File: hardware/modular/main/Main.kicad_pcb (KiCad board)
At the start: 4 copper layers, 80 x 125 mm, 246 parts, among them J1 TYPE-C-31-M-12, J10 Soldered wires Power_1x02, J2 Soldered wires Power_1x02, J3 Soldered wires Power_1x02, J4 Soldered wires Power_1x02, J6 Soldered wires Signal_2x04, J8 Soldered wires Signal_2x15, Q1 2N7002, Q2 2N7002, Q3 2N7002, SW1 RESET, SW2 BOOT, U1 TPD2EUSB30DRTR, U10 ADS7038IRTER, U11 TUSB320LAIRWBR, U12 TPS259470LRPWR, U13 TPS259470LRPWR, U14 SN74LVC2G04DCKR, U15 SN74LVC1G123DCUR, U16 SN74LVC08APWR, U17 SN74LVC08APWR, U18 SN74LVC08APWR, U19 TLV9001IDBVR, U2 TPS62162DSGR, U20 TPD2E2U06DCKR, U25 SN74LVC125APWR, U28 TPS22919DCKR, U29 SN74LVC125APWR, U3 ESP32-S3-MINI-1-N8, U32 ICM-42688-P, U33 TPS7A2450DBVR, U34 SN74LV1T34DBVR, U35 PMW3360DM-T2QU, U36 TLV75519PDBVR, U37 SN74LVC125APWR, U38 TPS22918DBVR, U39 SN74LVC1G125DBVR, U4 DRV8231ADSGR, U5 DRV8231ADSGR, U6 DRV8231ADSGR, U7 TMAG5253BA2IQDMRR, U8 TMAG5253BA2IQDMRR, U9 TMAG5253BA2IQDMRR

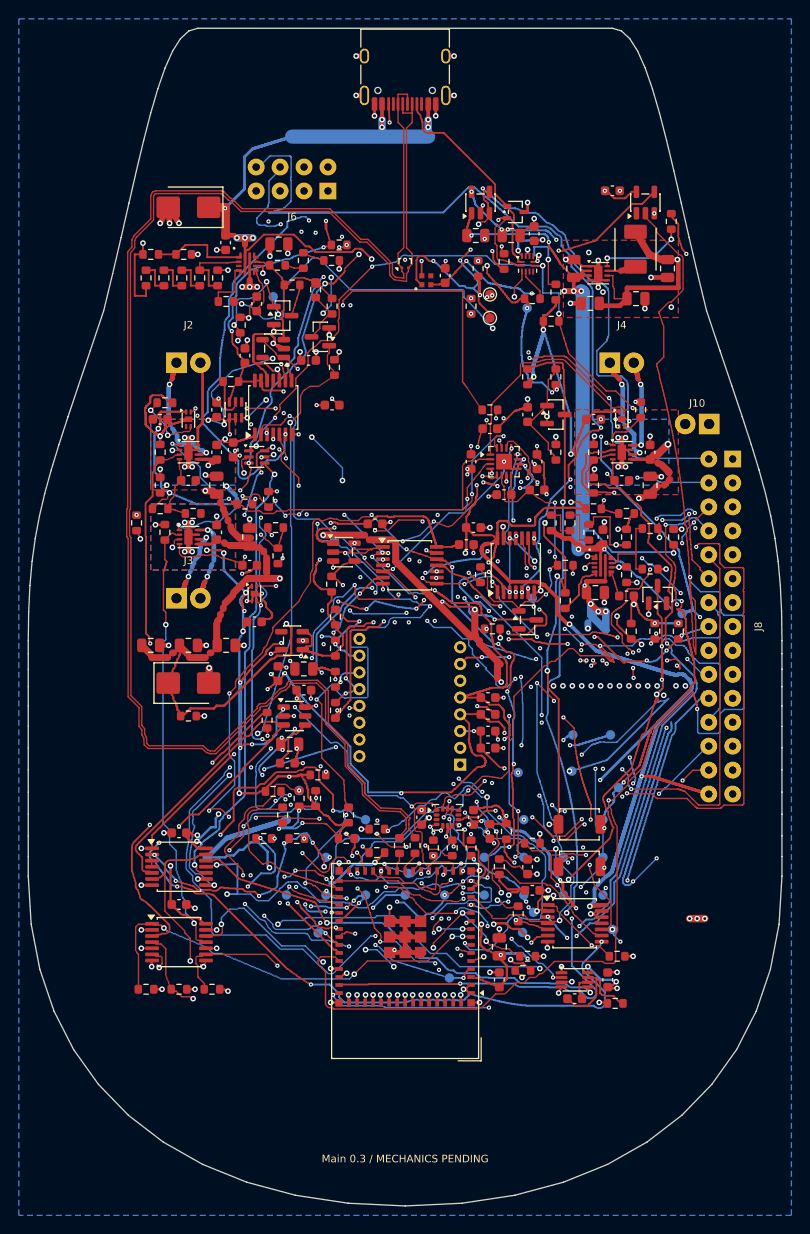
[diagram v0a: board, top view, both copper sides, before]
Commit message: Repair copper contacts and make manufacturing panel router-compatible
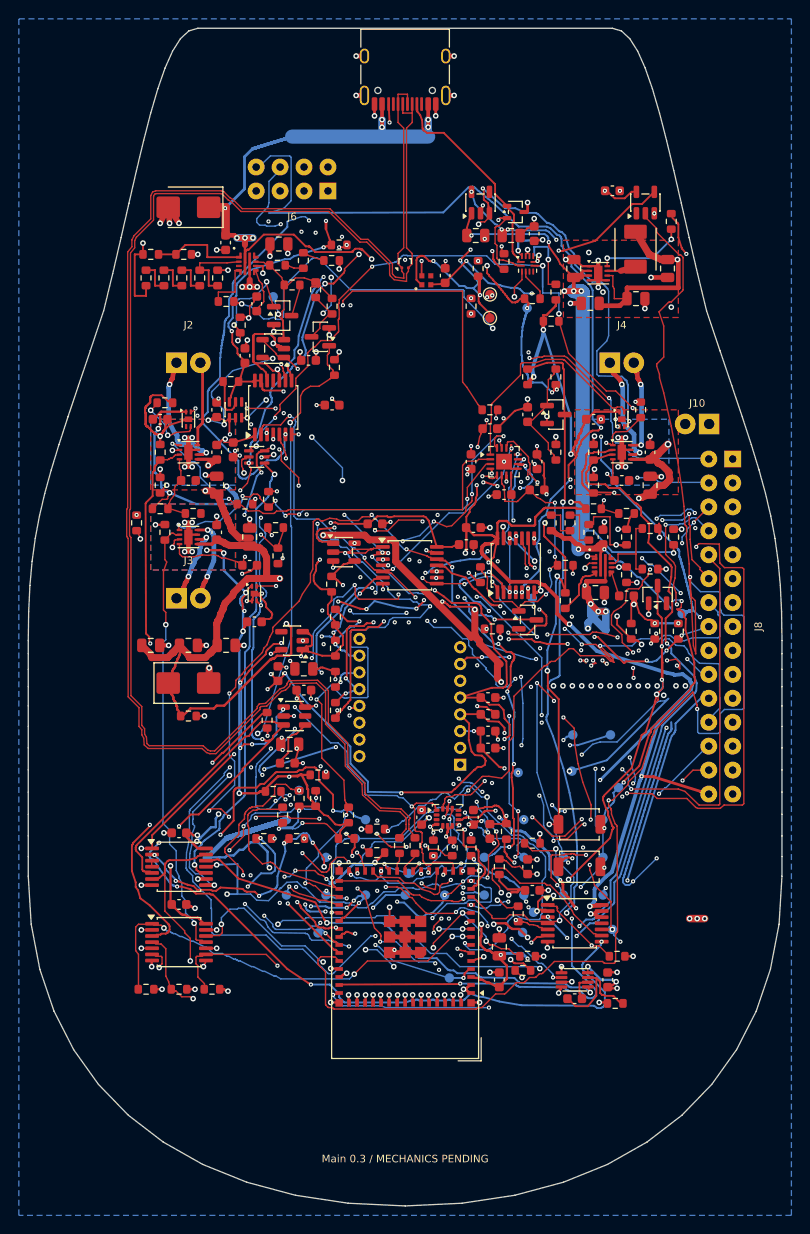
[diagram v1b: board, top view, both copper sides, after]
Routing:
- net ACT_5V: track 200.7 -> 360.5 mm
- net +3V3: track 589.9 -> 629.5 mm
- net VBUS_USB: track 148.2 -> 182.2 mm
- net HALL_EN: track 211.9 -> 241.7 mm
- net BTN_R_IN2: track 52.3 -> 73.3 mm
- net MCU_EN: track 179.4 -> 198.0 mm
- net GND: track 269.0 -> 286.6 mm
- net CC_OUT2: track 114.0 -> 130.8 mm
- net WHEEL_PWM_B: track 137.0 -> 153.2 mm
- net SPI_MOSI: track 192.6 -> 208.7 mm
- net OPT_CTRL: track 105.0 -> 121.0 mm
- net BTN_R_IN1: track 52.1 -> 67.9 mm
- net ACT_DRIVE_EN: track 120.6 -> 136.2 mm
- net CS_PAW: track 91.3 -> 106.7 mm
- net WHEEL_PWM_C: track 43.7 -> 57.7 mm
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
